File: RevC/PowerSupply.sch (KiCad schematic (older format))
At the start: 26 parts, among them Q21 DMG2301L, U22 TPS54202, U23 L7805, U24 MCP1754ST-3302E/CB, U25 NCP51460SN33T1G

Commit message: updates
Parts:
- added C?: 180pF, Resistor_SMD:R_0805_2012Metric_Pad1.15x1.40mm_HandSolder, symbol Device:C
- C1, C4: LcscNo (none) -> C14860; MouserNo 81-GRM21BC81C106KE5L -> (none)
- C11: LcscNo (none) -> C268007; MouserNo 810-C3216X5R1A476M -> (none); Type X5R, 2mΩ, 0.29A RMS, 4A -> X7R 25V
- C12: LcscNo (none) -> C268007; MouserNo 810-C3216X5R1A476M -> (none); Type X5R, 2mΩ, 0.29A RMS, 4A -> X5R 25V
- C2: LcscNo (none) -> C73142
- C29: value 1u MLCC 10V X7R -> 1u; LcscNo (none) -> C376927; MouserNo 80-C0805C105K3R -> (none); Type (none) -> 10V X7R
- C3: LcscNo (none) -> C94108
- C30: LcscNo (none) -> C94108; MouserNo 963-UMK212BJ104KG-T -> (none); Type (none) -> 10V
- C31: value 1u MLCC 10V X7R -> 1u; LcscNo (none) -> C376927; MouserNo 80-C0805C105K3R -> (none)
- C8: LcscNo (none) -> C152881; MouserNo 810-C3216X5R1A476M -> (none); Type (none) -> N/A
- C9: LcscNo (none) -> C94108; MouserNo 710-885012207098 -> (none); Type (none) -> X7R
- D13: LcscNo (none) -> C353516; MouserNo 771-BZT52-C5V1J -> (none); Type (none) -> Vz=5.1V
- L2: value 6.8uH -> 4.7uH; LcscNo (none) -> C266428; MouserNo 963-NRS8030T3R3MJGJ -> (none); Type (none) -> 3A
- Q21: value DMG2301L -> HX2301A; LcscNo (none) -> C296298; Type (none) -> VGS=+/-12V
- R13: LcscNo (none) -> C118844; MouserNo 71-CRCW080510K0FKEAC -> (none); Type (none) -> N/A
- R15: LcscNo (none) -> C118844; MouserNo 652-CR0805JW-563ELF -> (none); Type (none) -> N/A
- R16: Type (none) -> N/A
- R86: LcscNo (none) -> C118844; MouserNo 71-CRCW1206100KFKEAC -> (none); Type (none) -> N/A
- U22: value TPS54202 -> TPS54202DDCR; LcscNo (none) -> C191884; MouserNo 595-TPS54202DDCR -> (none)
- U23: LcscNo (none) -> C15077
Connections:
- net +10V_REG: now also C?.1
- net at C8.2, R15.1, R16.2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: now also C?.2
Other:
- moved on the sheet: C1, C11, C12, C2, C29, C3, C30, C31, C4, C8, C9, D13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

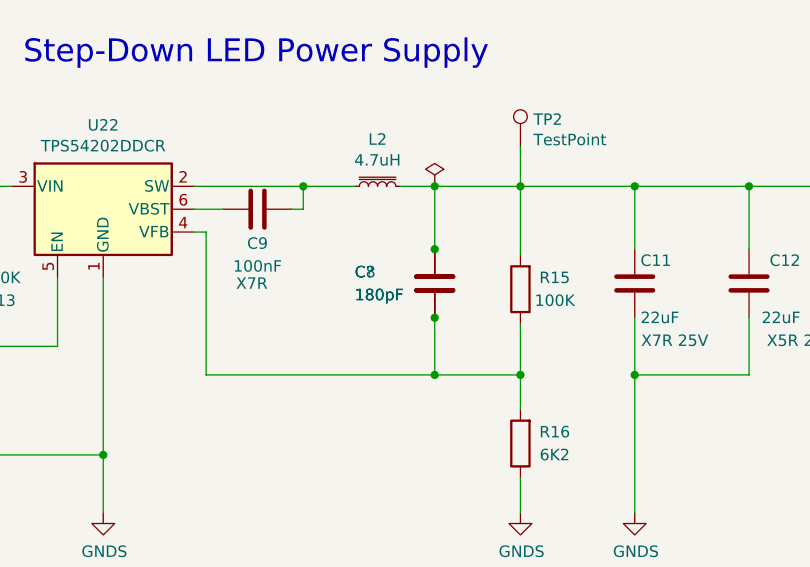
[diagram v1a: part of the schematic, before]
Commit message: Replaced 6N135 SMDIP8 with H11L1 SMDIP6
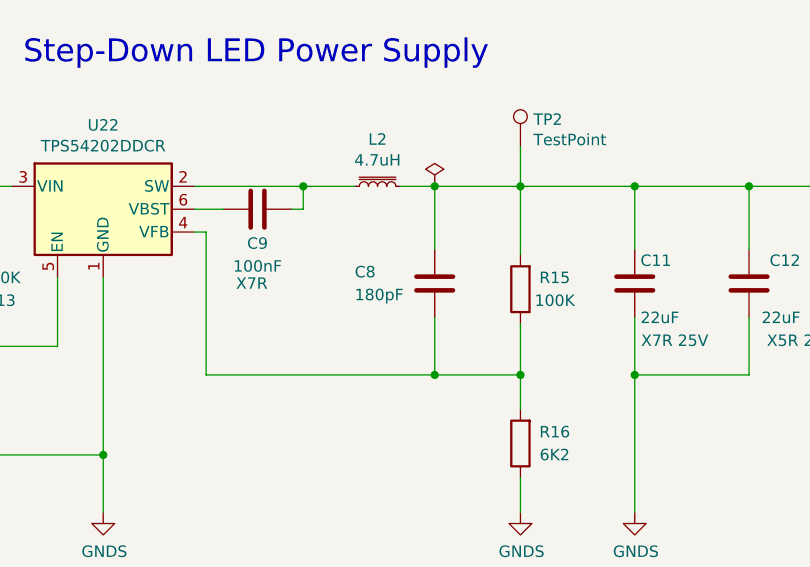
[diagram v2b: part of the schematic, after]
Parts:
- removed C?: 180pF, Resistor_SMD:R_0805_2012Metric_Pad1.15x1.40mm_HandSolder, symbol Device:C
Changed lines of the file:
@@
 	1    0    0    -1
 $EndComp
-$Comp
-L Device:C C?
-U 1 1 5E882806
-P 4000 4100
-AR Path="/5E882806" Ref="C?"  Part="1"
-AR Path="/5DEF0009/5E882806" Ref="C?"  Part="1"
-F 0 "C?" H 3650 4150 50  0000 L CNN
-F 1 "180pF" H 3650 4050 50  0000 L CNN
-F 2 "Resistor_SMD:R_0805_2012Metric_Pad1.15x1.40mm_HandSolder" H 4038 3950 50  0001 C CNN
-F 3 "~" H 4000 4100 50  0001 C CNN
-F 4 "N/A" H 4000 4100 50  0001 C CNN "Type"
-F 5 "C152881" H 4000 4100 50  0001 C CNN "LcscNo"
-	1    4000 4100
-	1    0    0    -1
-$EndComp
-Connection ~ 4000 3950
-Connection ~ 4000 4250
 $EndSCHEMATC

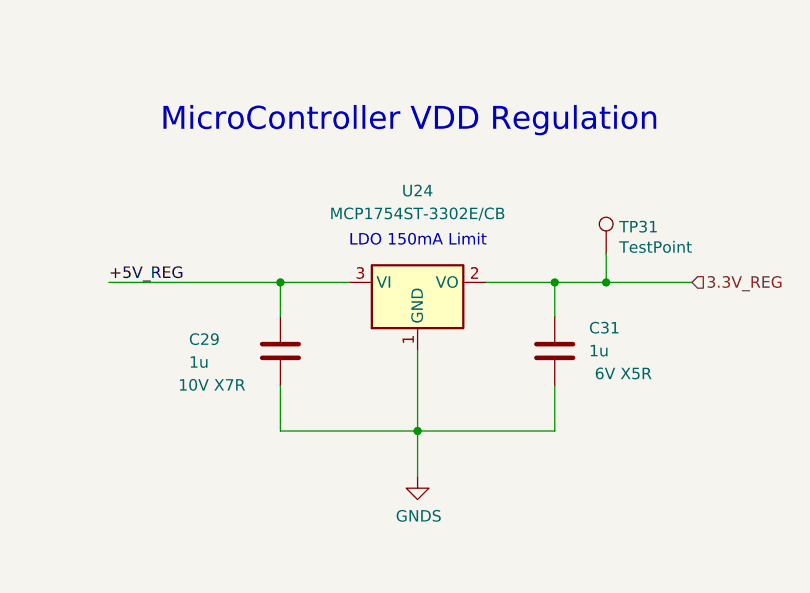
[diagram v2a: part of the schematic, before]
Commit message: hw update
switched MCP1754 (SOT23-3) to LP3992 (SOT23-5)
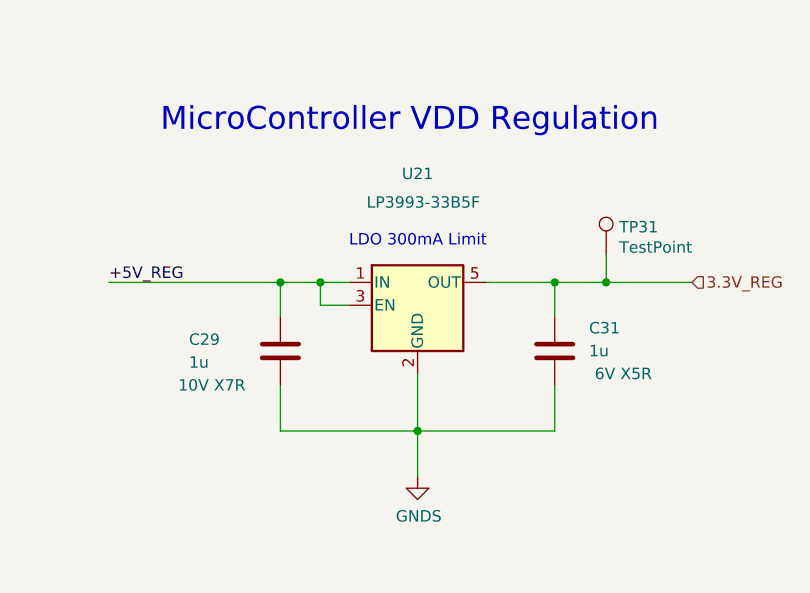
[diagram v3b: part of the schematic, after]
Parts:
- removed U24: MCP1754ST-3302E/CB, Package_TO_SOT_SMD:SOT-23, symbol Regulator_Linear:MCP1754S-3302xCB
- added U21: LP3993-33B5F, Package_TO_SOT_SMD:SOT-23-5, symbol Regulator_Linear:TLV70033_SOT23-5
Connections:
- net +5V_REG: now also U21.1 (IN), U21.3 (EN)
- net 3.3V_REG: now also U21.5 (OUT)
- net GNDS: now also U21.2 (GND)
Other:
- note added: "LDO 300mA Limit"
- note removed: "LDO 150mA Limit"
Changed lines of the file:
@@
 	9650 2300 9350 2300
 Wire Wire Line
-	8750 2300 8450 2300
+	8750 2300 8625 2300
 Wire Wire Line
 	8450 2300 8450 2450
 Wire Wire Line
-	9050 2600 9050 2950
+	9050 2700 9050 2950
 Wire Wire Line
 	9050 2950 8450 2950
@@
 Connection ~ 8450 2300
 Text Notes 8750 2150 0    50   ~ 0
-LDO 150mA Limit
+LDO 300mA Limit
 Wire Wire Line
 	9100 5225 9100 5375
@@
 	9775 4925 10050 4925
 $Comp
-L Regulator_Linear:MCP1754S-3302xCB U24
-U 1 1 5DBC0872
-P 9050 2300
-F 0 "U24" H 9050 2700 50  0000 C CNN
-F 1 "MCP1754ST-3302E/CB" H 9050 2600 50  0000 C CNN
-F 2 "Package_TO_SOT_SMD:SOT-23" H 9050 2525 50  0001 C CNN
-F 3 "http://ww1.microchip.com/downloads/en/DeviceDoc/20002276C.pdf" H 9050 2300 50  0001 C CNN
-F 4 "579-MCP1754T-3302ECB" H 9050 2300 50  0001 C CNN "MouserNo"
-	1    9050 2300
-	1    0    0    -1
-$EndComp
-$Comp
 L Transistor_FET:DMG2301L Q21
 U 1 1 5DCE743F
@@
 	1    0    0    -1
 $EndComp
+$Comp
+L Regulator_Linear:TLV70033_SOT23-5 U21
+U 1 1 5E7EEDCF
+P 9050 2400
+F 0 "U21" H 9050 2975 50  0000 C CNN
+F 1 "LP3993-33B5F" H 9075 2850 50  0000 C CNN
+F 2 "Package_TO_SOT_SMD:SOT-23-5" H 9050 2725 50  0001 C CIN
+F 3 "https://datasheet.lcsc.com/szlcsc/1811081106_LOWPOWER-LP3992-33B5F_C324570.pdf" H 9050 2450 50  0001 C CNN
+	1    9050 2400
+	1    0    0    -1
+$EndComp
+Wire Wire Line
+	8750 2400 8625 2400
+Wire Wire Line
+	8625 2400 8625 2300
+Connection ~ 8625 2300
+Wire Wire Line
+	8625 2300 8450 2300
 $EndSCHEMATC
